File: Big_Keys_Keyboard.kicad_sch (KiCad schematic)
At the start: 9 parts, among them U1 MX1A-11NN, U2 MX1A-11NN, U3 MX1A-11NN, U4 MX1A-11NN

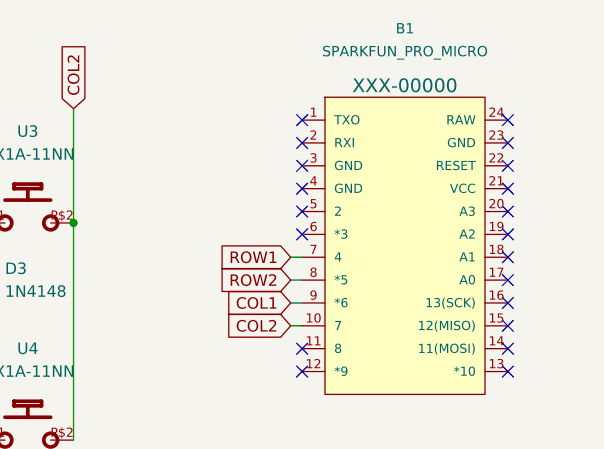
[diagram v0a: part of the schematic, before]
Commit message: track width changed to 0.5mm and zones filled with ground net
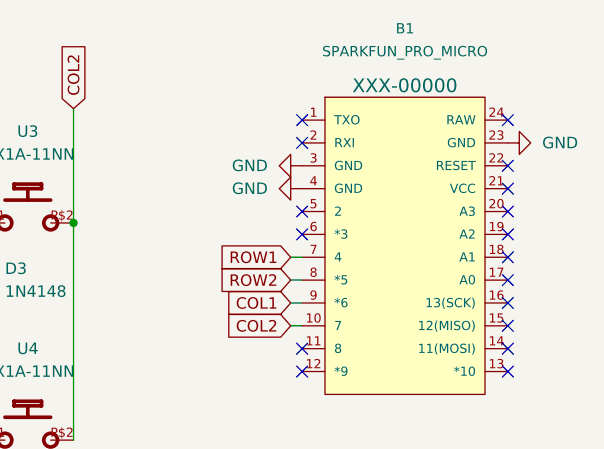
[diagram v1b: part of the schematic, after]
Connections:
- net GND: now reaches B1.23 (GND)
- net GND: now also B1.3 (GND), B1.4 (GND)
- no-connect marks 20 -> 17
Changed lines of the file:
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@@
   (no_connect (at 193.04 92.71))
   (no_connect (at 193.04 107.95))
-  (no_connect (at 170.18 87.63))
   (no_connect (at 193.04 102.87))
   (no_connect (at 170.18 82.55))
   (no_connect (at 170.18 85.09))
   (no_connect (at 193.04 100.33))
-  (no_connect (at 170.18 90.17))
   (no_connect (at 193.04 97.79))
   (no_connect (at 193.04 105.41))
-  (no_connect (at 193.04 85.09))
   (no_connect (at 193.04 110.49))
   (no_connect (at 193.04 95.25))
@@
     (pin "P$2")
   )
+  (symbol (lib_id "power:GND") (at 193.04 85.09 90) (unit 1)
+    (in_bom yes) (on_board yes) (fields_autoplaced)
+    (property "Reference" "#PWR?" (id 0) (at 199.39 85.09 0)
+      (effects (font (size 1.27 1.27)) hide)
+    )
+    (property "Value" "GND" (id 1) (at 196.85 85.0899 90)
+      (effects (font (size 1.27 1.27)) (justify right))
+    )
+    (property "Footprint" "" (id 2) (at 193.04 85.09 0)
+      (effects (font (size 1.27 1.27)) hide)
+    )
+    (property "Datasheet" "" (id 3) (at 193.04 85.09 0)
+      (effects (font (size 1.27 1.27)) hide)
+    )
+    (pin "1")
+  )
   (symbol (lib_id "MX1A-11NN:MX1A-11NN") (at 139.7 93.98 0) (unit 1)
     (in_bom yes) (on_board yes) (fields_autoplaced)
@@
     (pin "A")
     (pin "C")
+  )
+  (symbol (lib_id "power:GND") (at 170.18 90.17 270) (unit 1)
+    (in_bom yes) (on_board yes) (fields_autoplaced)
+    (property "Reference" "#PWR?" (id 0) (at 163.83 90.17 0)
+      (effects (font (size 1.27 1.27)) hide)
+    )
+    (property "Value" "GND" (id 1) (at 166.37 90.1699 90)
+      (effects (font (size 1.27 1.27)) (justify right))
+    )
+    (property "Footprint" "" (id 2) (at 170.18 90.17 0)
+      (effects (font (size 1.27 1.27)) hide)
+    )
+    (property "Datasheet" "" (id 3) (at 170.18 90.17 0)
+      (effects (font (size 1.27 1.27)) hide)
+    )
+    (pin "1")
   )
   (symbol (lib_id "SparkFun-Boards:SPARKFUN_PRO_MICRO") (at 181.61 96.52 0) (unit 1)
@@
     (pin "9")
   )
+  (symbol (lib_id "power:GND") (at 170.18 87.63 270) (unit 1)
+    (in_bom yes) (on_board yes) (fields_autoplaced)
+    (property "Reference" "#PWR?" (id 0) (at 163.83 87.63 0)
+      (effects (font (size 1.27 1.27)) hide)
+    )
+    (property "Value" "GND" (id 1) (at 166.37 87.6299 90)
+      (effects (font (size 1.27 1.27)) (justify right))
+    )
+    (property "Footprint" "" (id 2) (at 170.18 87.63 0)
+      (effects (font (size 1.27 1.27)) hide)
+    )
+    (property "Datasheet" "" (id 3) (at 170.18 87.63 0)
+      (effects (font (size 1.27 1.27)) hide)
+    )
+    (pin "1")
+  )
   (sheet_instances
     (path "/" (page "1"))
   )
   (symbol_instances
+    (path "/2e1299a3-9e9f-41b7-a996-d8c64efcd670"
+      (reference "#PWR?") (unit 1) (value "GND") (footprint "")
+    )
+    (path "/c7a8418b-4dad-4c61-b2ed-5f5bb50e4a1b"
+      (reference "#PWR?") (unit 1) (value "GND") (footprint "")
+    )
+    (path "/fa809503-fb3a-4963-8fb2-96fb54710cfd"
+      (reference "#PWR?") (unit 1) (value "GND") (footprint "")
+    )
     (path "/f9aa75fd-a63f-4e76-aa2f-f8f6eef366c4"
       (reference "B1") (unit 1) (value "SPARKFUN_PRO_MICRO") (footprint "Boards:SPARKFUN_PRO_MICRO")
